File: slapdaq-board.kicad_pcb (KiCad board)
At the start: 4 copper layers, 67 parts, among them J3 USB-C, Q1 BSS84, U1 LM2675M-3.3, U2 LM2675M-5, U3 ESP32-S3, U4 DT1042-04SO-7, U5 REF3333, U6 ADS1261, U7 MAX31856

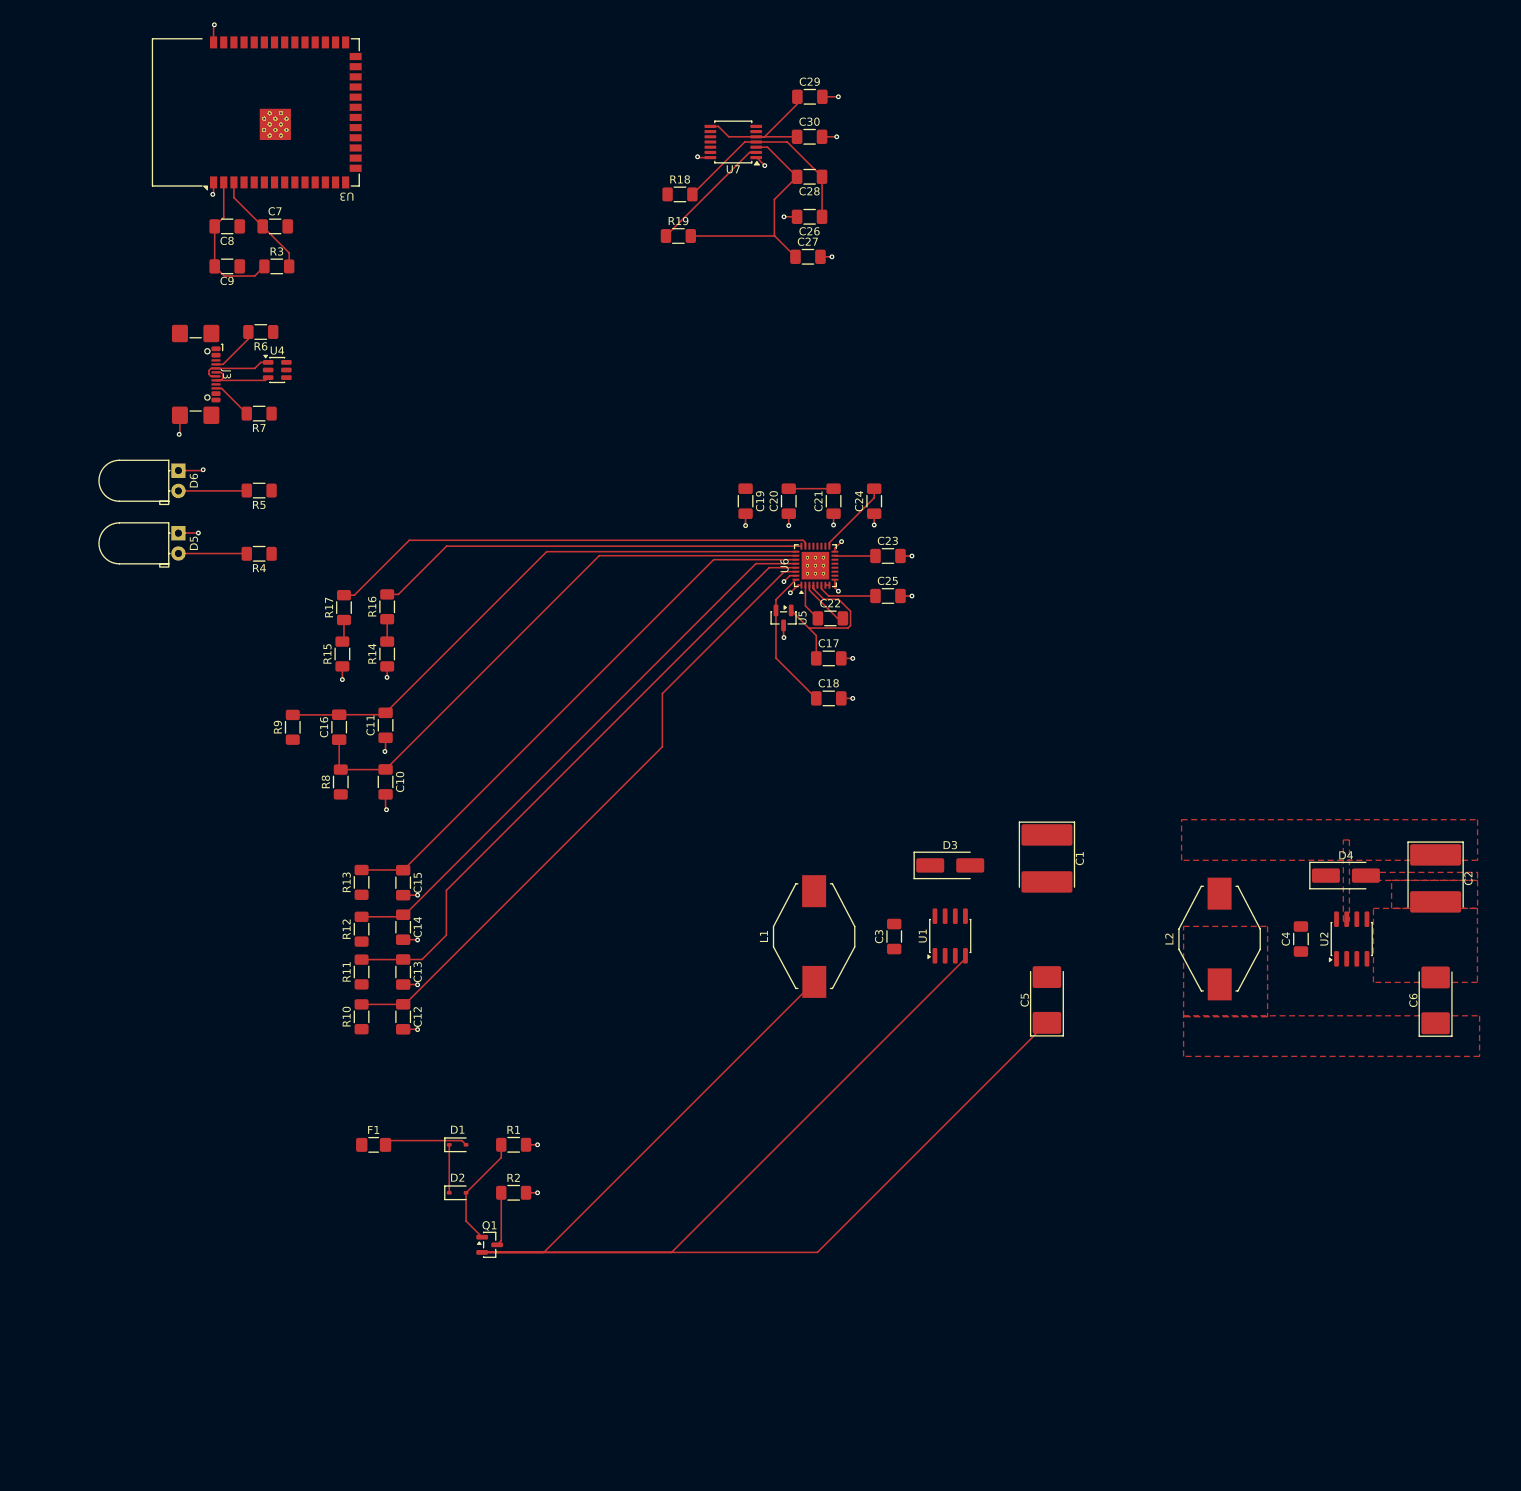
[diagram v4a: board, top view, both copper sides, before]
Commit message: did fills for voltages
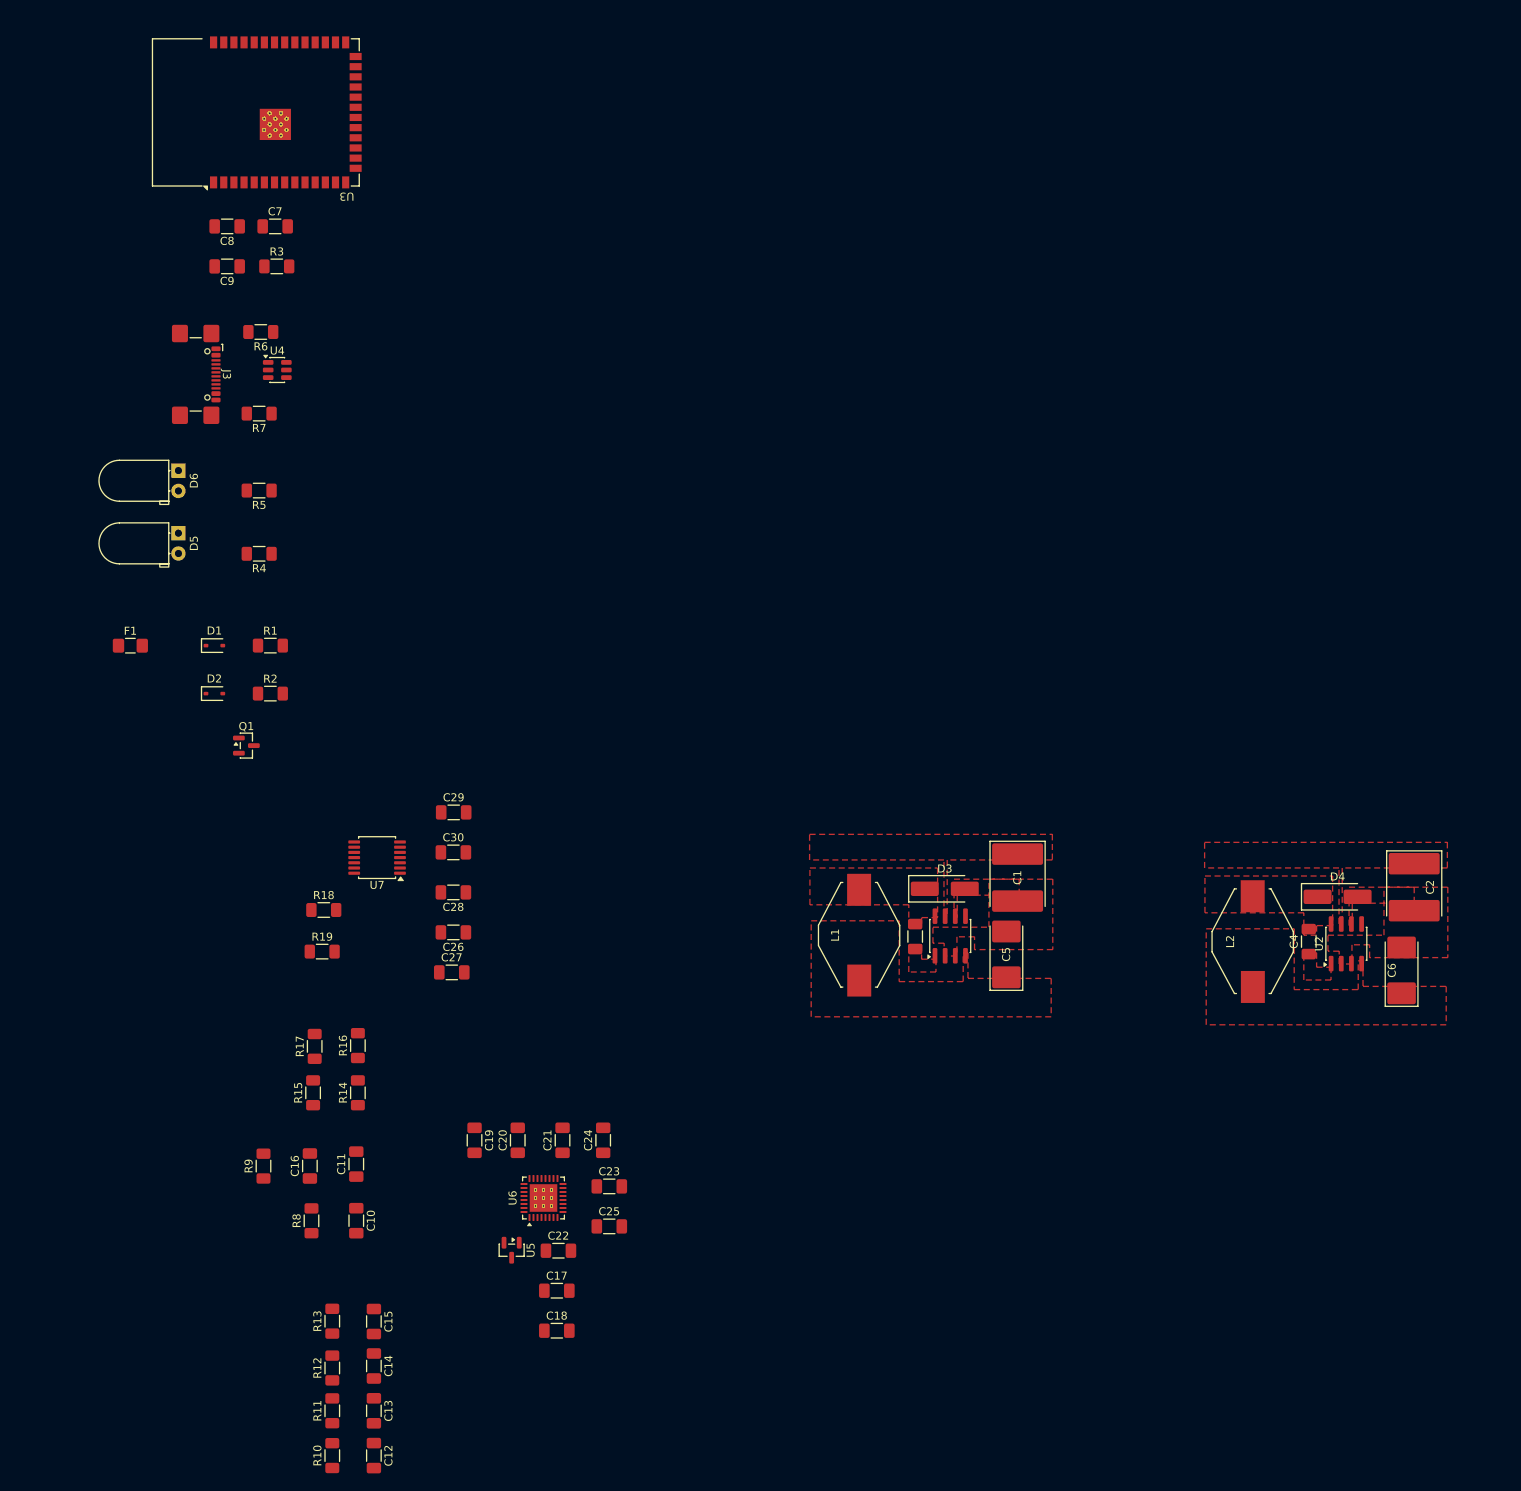
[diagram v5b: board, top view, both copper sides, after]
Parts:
- moved C26 99.9 mm to (79.5, 151.2)
- moved C27 99.9 mm to (79.3, 156.2)
- moved C28 99.9 mm to (79.5, 146.2)
- moved C29 99.9 mm to (79.5, 136.2)
- moved C30 99.9 mm to (79.5, 141.2)
- moved R19 99.9 mm to (63.1, 153.7)
- moved U7 99.9 mm to (69.9, 141.9)
- moved R18 99.9 mm to (63.3, 148.4)
- moved C20 86.8 mm to (87.5, 177.2)
- moved C24 86.8 mm to (98.2, 177.2)
- moved C19 86.8 mm to (82.1, 177.2)
- moved C21 86.8 mm to (93.1, 177.2)
- moved C23 86.2 mm to (99.0, 183.0)
- moved C25 86.2 mm to (99.0, 188.0)
- moved C17 86.0 mm to (92.4, 196.0)
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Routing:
- net +3.3V: track 261.8 -> 0.00 mm
- net Net-(U6-AIN2): track 80.6 -> 0.00 mm
- net Net-(U6-AIN3): track 77.9 -> 0.00 mm
- net Net-(U6-AIN4): track 72.6 -> 0.00 mm
- net Net-(U6-AIN7): track 72.0 -> 0.00 mm
- net Net-(U6-AIN6): track 71.8 -> 0.00 mm
- net Net-(U6-AIN5): track 70.4 -> 0.00 mm
- net Net-(U6-AIN9): track 61.1 -> 0.00 mm
- net GND: track 59.6 -> 0.00 mm, vias 34 -> 0
- net Net-(U6-AIN8): track 54.3 -> 0.00 mm
- net Net-(U7-T-): track 29.4 -> 0.00 mm
- net +5V: track 26.9 -> 0.00 mm
- net Net-(U7-T+): track 25.7 -> 0.00 mm
- net Net-(U5-OUT): track 18.0 -> 0.00 mm
- net Net-(J7-Pin_2): track 15.6 -> 0.00 mm
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- added copper zone on F.Cu, net +3.3V
- added copper zone on F.Cu, net +5V
- added copper zone on F.Cu, net Net-(D3-K)
- added copper zone on F.Cu, net Net-(U1-CB)

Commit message: Add screw terminals
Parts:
- added J1: Higher Screw Terminals, Custom_Footprints:CONN_SD-39512-001_10P_MOL, F.Cu at (33.0, 134.3)
- added J2: Lower Screw Terminals, Custom_Footprints:CONN_SD-39512-001_10P_MOL, F.Cu at (33.0, 182.0)
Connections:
- net Net-(J6-Pin_1) renamed C1
- net Net-(J6-Pin_2) renamed C2
- net Net-(J7-Pin_2) renamed TH-
- F1 pad 1: Net-(J1-Pin_1) -> +12V
- R10 pad 1: Net-(J4-Pin_1) -> AV1
- R11 pad 1: Net-(J4-Pin_2) -> AV2
- R12 pad 1: Net-(J4-Pin_3) -> AV3
- R13 pad 1: Net-(J4-Pin_4) -> AV4
- R18 pad 1: Net-(J7-Pin_1) -> TH+
- R8 pad 1: Net-(J5-Pin_1) -> DV+
- R9 pad 1: Net-(J5-Pin_2) -> DV-
- U3 pad 10: /MCU/DIO7 -> DIO7
- U3 pad 11: /MCU/DIO8 -> DIO8
- U3 pad 4: /MCU/DIO1 -> DIO1
- U3 pad 5: /MCU/DIO2 -> DIO2
- U3 pad 6: /MCU/DIO3 -> DIO3
- U3 pad 7: /MCU/DIO4 -> DIO4
- U3 pad 8: /MCU/DIO5 -> DIO5
- U3 pad 9: /MCU/DIO6 -> DIO6

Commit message: Add 3D models and rearrange pins
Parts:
- added NT1: NetTie_2, NetTie:NetTie-2_SMD_Pad0.5mm, F.Cu at (66.0, 80.2)
- moved U2 11.8 mm to (179.4, 151.7)
- moved C2 11.7 mm to (187.9, 144.2)
- moved L2 11.7 mm to (167.8, 151.2)
- moved C4 11.5 mm to (174.9, 151.2)
- moved D4 11.4 mm to (178.7, 145.6)
- moved C6 10.1 mm to (187.9, 155.5)
- moved C5 2.04 mm to (150.0, 155.5)
- moved C1 0.35 mm to (150.0, 144.1)
- moved D3 0.10 mm to (141.0, 145.8)
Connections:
- J1 pad 1: DIO1 -> DIO0
- J1 pad 2: DIO2 -> DIO1
- J1 pad 3: DIO3 -> DIO2
- J1 pad 4: DIO4 -> DIO3
- J1 pad 5: DIO5 -> DIO4
- J1 pad 6: DIO6 -> DIO5
- J1 pad 7: DIO7 -> DIO6
- J1 pad 8: DIO8 -> DIO7
- J2 pad 1: AV1 -> AC1
- J2 pad 2: AV2 -> AC2
- J2 pad 3: AV3 -> DV+
- J2 pad 4: AV4 -> DV-
- J2 pad 5: DV+ -> AV1
- J2 pad 6: DV- -> AV2
- J2 pad 7: C1 -> AV3
- J2 pad 8: C2 -> AV4
- R10 pad 1: AV1 -> AV4
- R11 pad 1: AV2 -> AV3
- R12 pad 1: AV3 -> AV2
- R13 pad 1: AV4 -> AV1
- R14 pad 2: C1 -> AC2
- R15 pad 2: C2 -> AC1
- R16 pad 1: C1 -> AC2
- R17 pad 1: C2 -> AC1
- R8 pad 1: DV+ -> DV-
- R9 pad 1: DV- -> DV+
- U3 pad 10: DIO7 -> DIO6
- U3 pad 11: DIO8 -> DIO7
- U3 pad 4: DIO1 -> DIO0
- U3 pad 5: DIO2 -> DIO1
- U3 pad 6: DIO3 -> DIO2
- U3 pad 7: DIO4 -> DIO3
- U3 pad 8: DIO5 -> DIO4
- U3 pad 9: DIO6 -> DIO5
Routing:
- added copper zone on F.Cu, net Net-(D4-K)
- added copper zone on F.Cu, net Net-(Q1-D)
- added copper zone on F.Cu, net Net-(U2-CB)

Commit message: pcb trace work
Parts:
- removed NT1: NetTie_2, NetTie:NetTie-2_SMD_Pad0.5mm
- moved D1 79.0 mm to (49.2, 194.4), turned to 180 degrees
- moved F1 76.2 mm to (50.0, 190.8)
- moved R1 75.4 mm to (56.0, 190.8)
- moved D2 73.1 mm to (53.4, 194.4)
- moved R2 69.6 mm to (61.6, 190.8), turned to 180 degrees
- moved Q1 59.3 mm to (63.0, 186.4)
- moved C1 38.7 mm to (163.5, 180.3)
- moved C3 38.7 mm to (150.7, 188.0)
- moved C5 38.7 mm to (163.5, 191.7)
- moved D3 38.7 mm to (154.5, 182.1)
- moved L1 38.7 mm to (143.7, 187.8)
- moved U1 38.7 mm to (155.1, 187.9)
- moved C4 38.0 mm to (187.4, 187.0)
- moved C6 38.0 mm to (200.4, 191.4)
- moved D4 38.0 mm to (191.2, 181.4)
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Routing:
- net SPI_D: track 0.00 -> 144.7 mm, vias 0 -> 3
- net SPI_Q: track 0.00 -> 143.4 mm, vias 0 -> 4
- net SPI_CLK: track 0.00 -> 137.0 mm, vias 0 -> 4
- net CS0_ADC: track 0.00 -> 134.4 mm, vias 0 -> 2
- net CS1_THR: track 0.00 -> 108.0 mm, vias 0 -> 2
- net DIO7: track 0.00 -> 91.3 mm, vias 0 -> 2
- net DIO6: track 0.00 -> 87.1 mm, vias 0 -> 2
- net DIO5: track 0.00 -> 82.7 mm, vias 0 -> 2
- net DIO4: track 0.00 -> 78.4 mm, vias 0 -> 2
- net DIO3: track 0.00 -> 74.1 mm, vias 0 -> 2
- net DIO2: track 0.00 -> 69.7 mm, vias 0 -> 2
- net Net-(U6-CAPP): track 0.00 -> 65.6 mm
- net DIO1: track 0.00 -> 65.4 mm, vias 0 -> 2
- net /MCU/WIFI_LED: track 0.00 -> 61.6 mm, vias 0 -> 2
- net DIO0: track 0.00 -> 61.1 mm, vias 0 -> 2
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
